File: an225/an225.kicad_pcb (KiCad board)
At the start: 2 copper layers, 77.3 x 70.3 mm, 1 part

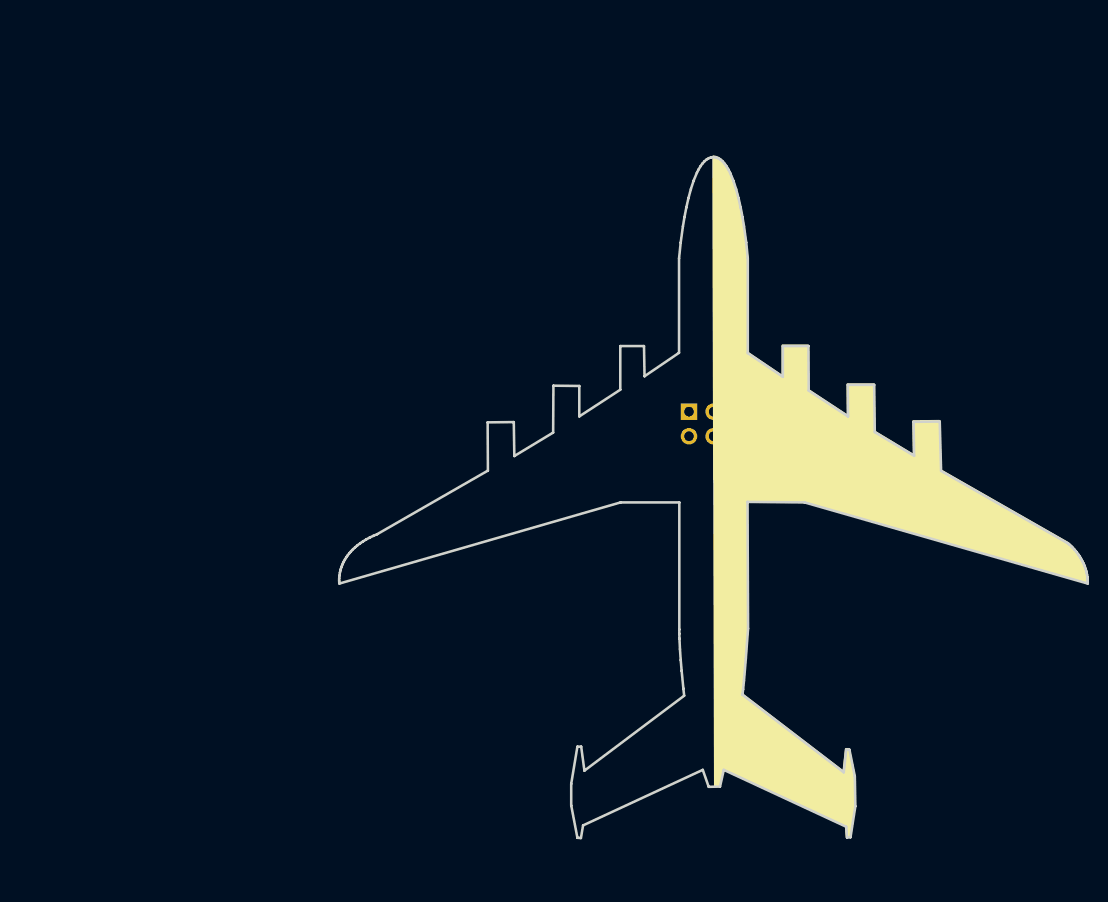
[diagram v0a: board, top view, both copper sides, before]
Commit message: v2 of AN225 SAO that uses a computer traced image for the badge instead of hand drawn
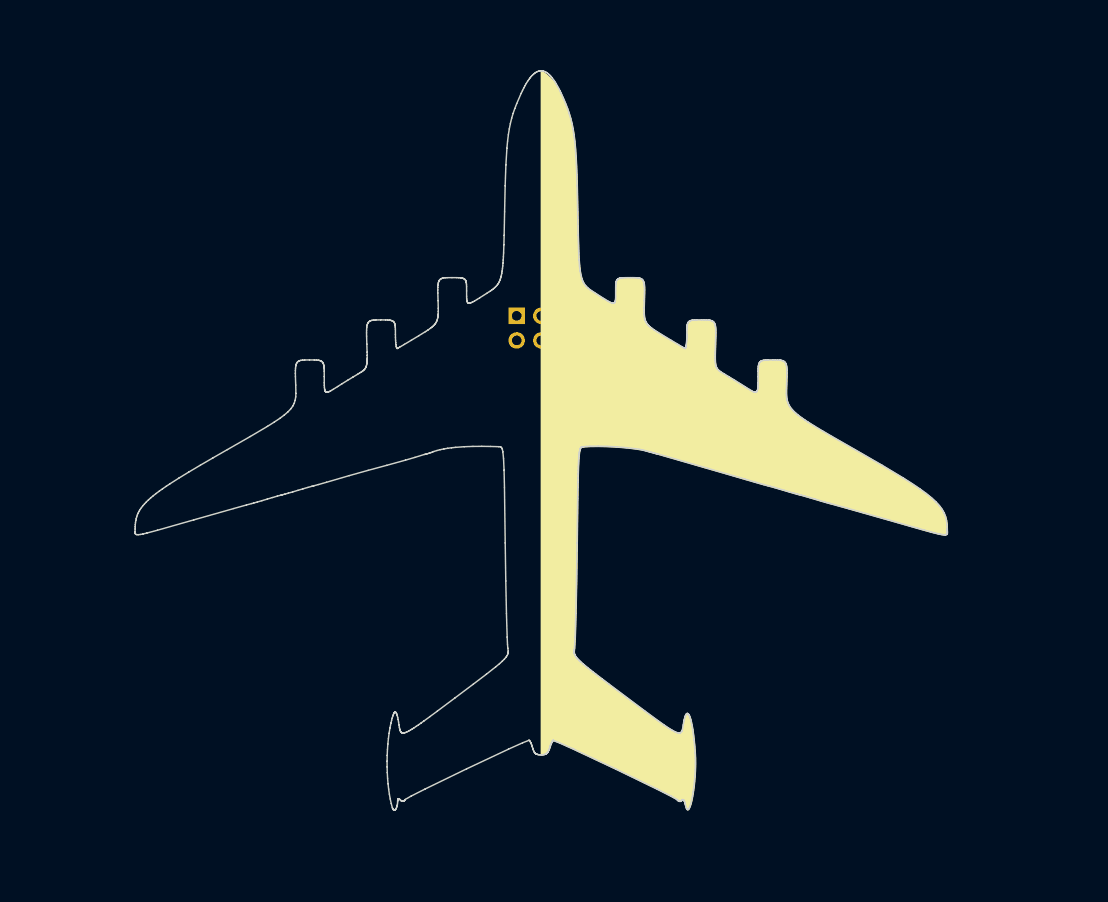
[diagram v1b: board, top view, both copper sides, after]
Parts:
- moved REF** 20.4 mm to (117.4, 71.2)
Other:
- board size 77.3 x 70.3 mm -> 83.9 x 76.4 mm
- board text added: "jlcjlcjlcjlc"
- board text added: "v2"

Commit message: updated AN225 SAO
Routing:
- added copper zone on B.Cu, net (none)
- added copper zone on F.Cu, net (none)
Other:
- board text removed: "jlcjlcjlcjlc"
